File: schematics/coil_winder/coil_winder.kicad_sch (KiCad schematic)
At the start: 2 parts, among them SW1 RotaryEncoder_Switch, U1 Pico

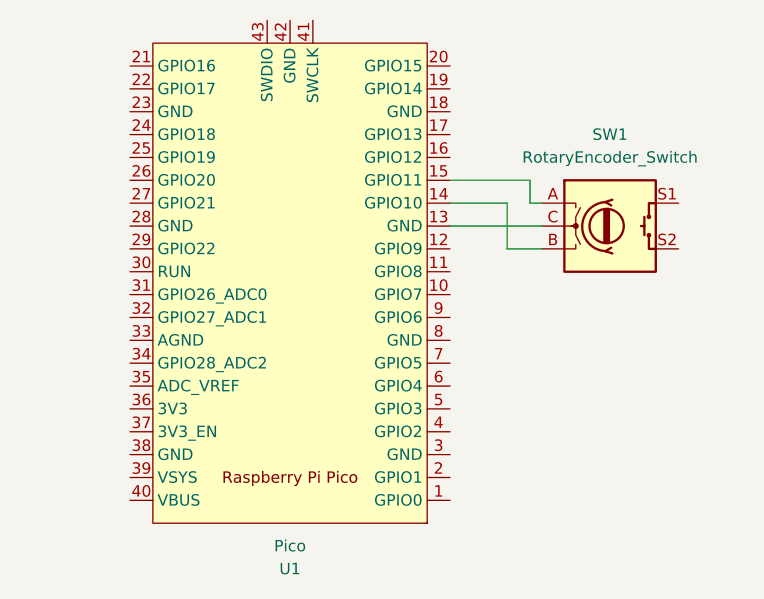
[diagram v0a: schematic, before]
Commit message: Update schematic to include I2C LCD
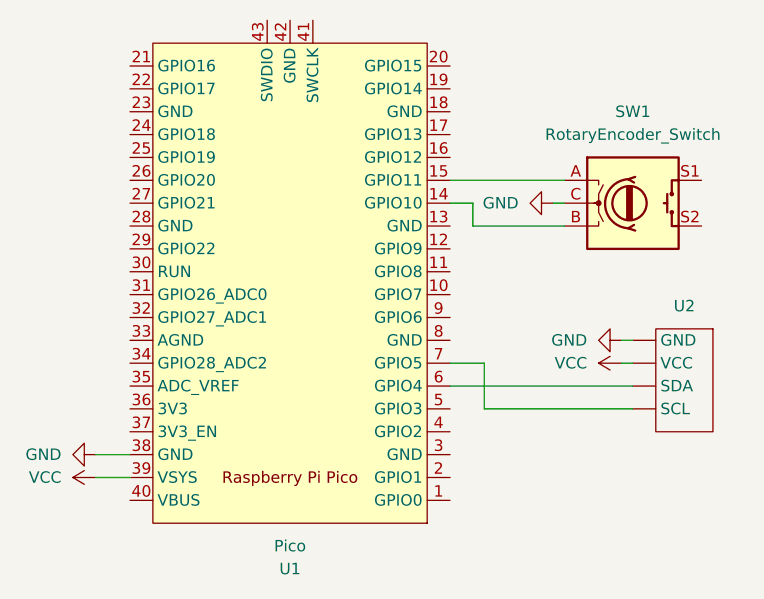
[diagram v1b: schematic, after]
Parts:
- added U2: ~, symbol MCU_RaspberryPi_and_Boards:I2C_LCD
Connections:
- net at U1.13 (GND): no longer SW1.C
- net GND: now reaches U1.38 (GND)
- net GND: now also SW1.C, U2. (VCC)
- net VCC: now reaches U1.39 (VSYS)
- net VCC: now also U2. (VCC)
- net at U1.6 (GPIO4): now also U2. (VCC)
- net at U1.7 (GPIO5): now also U2. (VCC)
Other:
- moved on the sheet: SW1
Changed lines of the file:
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@@
 (kicad_sch (version 20230121) (generator eeschema)
   (paper "A4")
-  (wire (pts (xy 158.75 78.74) (xy 158.75 73.66))
-    (stroke (width 0) (type default))
-  )
-  (wire (pts (xy 158.75 73.66) (xy 152.4 73.66))
-    (stroke (width 0) (type default))
-  )
-  (wire (pts (xy 162.56 73.66) (xy 161.29 73.66))
-    (stroke (width 0) (type default))
-  )
-  (wire (pts (xy 152.4 76.2) (xy 162.56 76.2))
-    (stroke (width 0) (type default))
-  )
-  (wire (pts (xy 161.29 71.12) (xy 152.4 71.12))
-    (stroke (width 0) (type default))
-  )
-  (wire (pts (xy 161.29 73.66) (xy 161.29 71.12))
-    (stroke (width 0) (type default))
-  )
-  (wire (pts (xy 162.56 78.74) (xy 158.75 78.74))
-    (stroke (width 0) (type default))
+  (wire (pts (xy 152.4 93.98) (xy 172.72 93.98))
+    (stroke (width 0) (type default))
+  )
+  (wire (pts (xy 113.03 104.14) (xy 116.84 104.14))
+    (stroke (width 0) (type default))
+  )
+  (wire (pts (xy 156.21 91.44) (xy 152.4 91.44))
+    (stroke (width 0) (type default))
+  )
+  (wire (pts (xy 154.94 73.66) (xy 152.4 73.66))
+    (stroke (width 0) (type default))
+  )
+  (wire (pts (xy 165.1 76.2) (xy 154.94 76.2))
+    (stroke (width 0) (type default))
+  )
+  (wire (pts (xy 156.21 96.52) (xy 156.21 91.44))
+    (stroke (width 0) (type default))
+  )
+  (wire (pts (xy 154.94 76.2) (xy 154.94 73.66))
+    (stroke (width 0) (type default))
+  )
+  (wire (pts (xy 171.45 91.44) (xy 172.72 91.44))
+    (stroke (width 0) (type default))
+  )
+  (wire (pts (xy 163.83 73.66) (xy 165.1 73.66))
+    (stroke (width 0) (type default))
+  )
+  (wire (pts (xy 113.03 101.6) (xy 116.84 101.6))
+    (stroke (width 0) (type default))
+  )
+  (wire (pts (xy 152.4 71.12) (xy 165.1 71.12))
+    (stroke (width 0) (type default))
+  )
+  (wire (pts (xy 172.72 96.52) (xy 156.21 96.52))
+    (stroke (width 0) (type default))
+  )
+  (wire (pts (xy 171.45 88.9) (xy 172.72 88.9))
+    (stroke (width 0) (type default))
+  )
+  (symbol (lib_id "power:VCC") (at 113.03 104.14 90) (unit 1)
+    (in_bom yes) (on_board yes) (dnp no) (fields_autoplaced)
+    (property "Reference" "#PWR04" (at 116.84 104.14 0)
+      (effects (font (size 1.27 1.27)) hide)
+    )
+    (property "Value" "VCC" (at 109.22 104.14 90)
+      (effects (font (size 1.27 1.27)) (justify left))
+    )
+    (property "Footprint" "" (at 113.03 104.14 0)
+      (effects (font (size 1.27 1.27)) hide)
+    )
+    (property "Datasheet" "" (at 113.03 104.14 0)
+      (effects (font (size 1.27 1.27)) hide)
+    )
+    (pin "1")
+    (instances
+      (project "coil_winder"
+        (path "/5ec64e02-ee9b-4809-b355-36a61de13204"
+          (reference "#PWR04") (unit 1)
+        )
+      )
+    )
+  )
+  (symbol (lib_id "power:VCC") (at 171.45 91.44 90) (unit 1)
+    (in_bom yes) (on_board yes) (dnp no) (fields_autoplaced)
+    (property "Reference" "#PWR05" (at 175.26 91.44 0)
+      (effects (font (size 1.27 1.27)) hide)
+    )
+    (property "Value" "VCC" (at 167.64 91.44 90)
+      (effects (font (size 1.27 1.27)) (justify left))
+    )
+    (property "Footprint" "" (at 171.45 91.44 0)
+      (effects (font (size 1.27 1.27)) hide)
+    )
+    (property "Datasheet" "" (at 171.45 91.44 0)
+      (effects (font (size 1.27 1.27)) hide)
+    )
+    (pin "1")
+    (instances
+      (project "coil_winder"
+        (path "/5ec64e02-ee9b-4809-b355-36a61de13204"
+          (reference "#PWR05") (unit 1)
+        )
+      )
+    )
+  )
+  (symbol (lib_id "MCU_RaspberryPi_and_Boards:I2C_LCD") (at 177.8 92.71 0) (mirror y) (unit 1)
+    (in_bom yes) (on_board yes) (dnp no)
+    (property "Reference" "U2" (at 178.435 85.09 0)
+      (effects (font (size 1.27 1.27)))
+    )
+    (property "Value" "~" (at 179.07 86.36 0)
+      (effects (font (size 1.27 1.27)))
+    )
+    (property "Footprint" "" (at 179.07 86.36 0)
+      (effects (font (size 1.27 1.27)) hide)
+    )
+    (property "Datasheet" "" (at 179.07 86.36 0)
+      (effects (font (size 1.27 1.27)) hide)
+    )
+    (pin "")
+    (pin "")
+    (pin "")
+    (pin "")
+    (instances
+      (project "coil_winder"
+        (path "/5ec64e02-ee9b-4809-b355-36a61de13204"
+          (reference "U2") (unit 1)
+        )
+      )
+    )
+  )
+  (symbol (lib_id "power:GND") (at 113.03 101.6 270) (unit 1)
+    (in_bom yes) (on_board yes) (dnp no) (fields_autoplaced)
+    (property "Reference" "#PWR03" (at 106.68 101.6 0)
+      (effects (font (size 1.27 1.27)) hide)
+    )
+    (property "Value" "GND" (at 109.22 101.6 90)
+      (effects (font (size 1.27 1.27)) (justify right))
+    )
+    (property "Footprint" "" (at 113.03 101.6 0)
+      (effects (font (size 1.27 1.27)) hide)
+    )
+    (property "Datasheet" "" (at 113.03 101.6 0)
+      (effects (font (size 1.27 1.27)) hide)
+    )
+    (pin "1")
+    (instances
+      (project "coil_winder"
+        (path "/5ec64e02-ee9b-4809-b355-36a61de13204"
+          (reference "#PWR03") (unit 1)
+        )
+      )
+    )
+  )
+  (symbol (lib_id "power:GND") (at 171.45 88.9 270) (unit 1)
+    (in_bom yes) (on_board yes) (dnp no) (fields_autoplaced)
+    (property "Reference" "#PWR02" (at 165.1 88.9 0)
+      (effects (font (size 1.27 1.27)) hide)
+    )
+    (property "Value" "GND" (at 167.64 88.9 90)
+      (effects (font (size 1.27 1.27)) (justify right))
+    )
+    (property "Footprint" "" (at 171.45 88.9 0)
+      (effects (font (size 1.27 1.27)) hide)
+    )
+    (property "Datasheet" "" (at 171.45 88.9 0)
+      (effects (font (size 1.27 1.27)) hide)
+    )
+    (pin "1")
+    (instances
+      (project "coil_winder"
+        (path "/5ec64e02-ee9b-4809-b355-36a61de13204"
+          (reference "#PWR02") (unit 1)
+        )
+      )
+    )
+  )
+  (symbol (lib_id "power:GND") (at 163.83 73.66 270) (unit 1)
+    (in_bom yes) (on_board yes) (dnp no) (fields_autoplaced)
+    (property "Reference" "#PWR01" (at 157.48 73.66 0)
+      (effects (font (size 1.27 1.27)) hide)
+    )
+    (property "Value" "GND" (at 160.02 73.66 90)
+      (effects (font (size 1.27 1.27)) (justify right))
+    )
+    (property "Footprint" "" (at 163.83 73.66 0)
+      (effects (font (size 1.27 1.27)) hide)
+    )
+    (property "Datasheet" "" (at 163.83 73.66 0)
+      (effects (font (size 1.27 1.27)) hide)
+    )
+    (pin "1")
+    (instances
+      (project "coil_winder"
+        (path "/5ec64e02-ee9b-4809-b355-36a61de13204"
+          (reference "#PWR01") (unit 1)
+        )
+      )
+    )
   )
   (symbol (lib_id "MCU_RaspberryPi_and_Boards:Pico") (at 134.62 82.55 180) (unit 1)
@@
     )
   )
-  (symbol (lib_id "Device:RotaryEncoder_Switch") (at 170.18 76.2 0) (unit 1)
+  (symbol (lib_id "Device:RotaryEncoder_Switch") (at 172.72 73.66 0) (unit 1)
     (in_bom yes) (on_board yes) (dnp no)
-    (property "Reference" "SW1" (at 170.18 66.04 0)
-      (effects (font (size 1.27 1.27)))
-    )
-    (property "Value" "RotaryEncoder_Switch" (at 170.18 68.58 0)
-      (effects (font (size 1.27 1.27)))
-    )
-    (property "Footprint" "" (at 166.37 72.136 0)
-      (effects (font (size 1.27 1.27)) hide)
-    )
-    (property "Datasheet" "~" (at 170.18 69.596 0)
-      (effects (font (size 1.27 1.27)) hide)
-    )
+    (property "Reference" "SW1" (at 172.72 63.5 0)
+      (effects (font (size 1.27 1.27)))
+    )
+    (property "Value" "RotaryEncoder_Switch" (at 172.72 66.04 0)
+      (effects (font (size 1.27 1.27)))
+    )
+    (property "Footprint" "" (at 168.91 69.596 0)
+      (effects (font (size 1.27 1.27)) hide)
+    )
+    (property "Datasheet" "~" (at 172.72 67.056 0)
+      (effects (font (size 1.27 1.27)) hide)
+    )

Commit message: Add stepper motors unconnected to pi
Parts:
- added A1, A2: Pololu_Breakout_A4988, Module:Pololu_Breakout-16_15.2x20.3mm, symbol Driver_Motor:Pololu_Breakout_A4988
- added J1: Stepper_Motor_1, symbol Connector_Generic:Conn_01x04
- added J2: Stepper_Motor_2, symbol Connector_Generic:Conn_01x04
- renumbered U2 to LCD
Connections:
- net GND: now also A1.1 (GND), A1.12 (MS3), A1.7 (GND), A2.1 (GND), A2.12 (MS3), A2.7 (GND)
- net VCC: now also A1.10 (MS1), A1.11 (MS2), A1.2 (VDD), A2.10 (MS1), A2.11 (MS2), A2.2 (VDD)
- new net: A1.3 (1B), J1.1 (Pin_1)
- new net: A1.4 (1A), J1.2 (Pin_2)
- new net: A1.5 (2A), J1.3 (Pin_3)
- new net: A1.6 (2B), J1.4 (Pin_4)
- new net: A1.13 (~{RESET}), A1.14 (~{SLEEP})
- new net: A2.3 (1B), J2.1 (Pin_1)
- new net: A2.4 (1A), J2.2 (Pin_2)
- new net: A2.5 (2A), J2.3 (Pin_3)
- new net: A2.6 (2B), J2.4 (Pin_4)
- new net: A2.13 (~{RESET}), A2.14 (~{SLEEP})
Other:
- moved on the sheet: LCD, SW1, U1

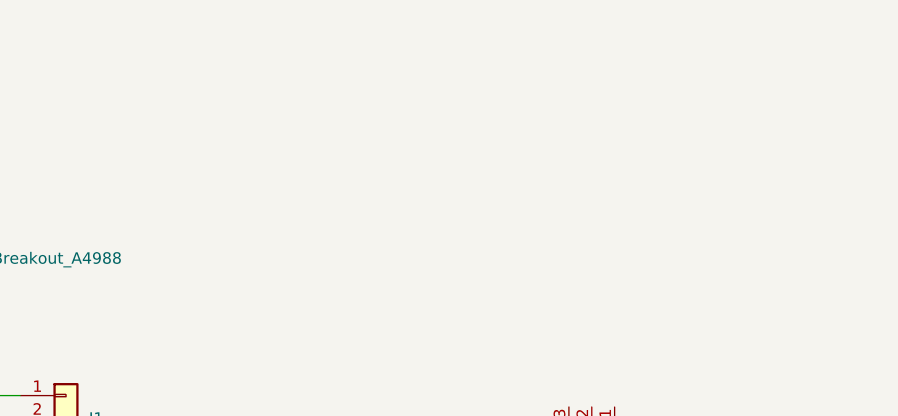
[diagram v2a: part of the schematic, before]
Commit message: Add power circuit
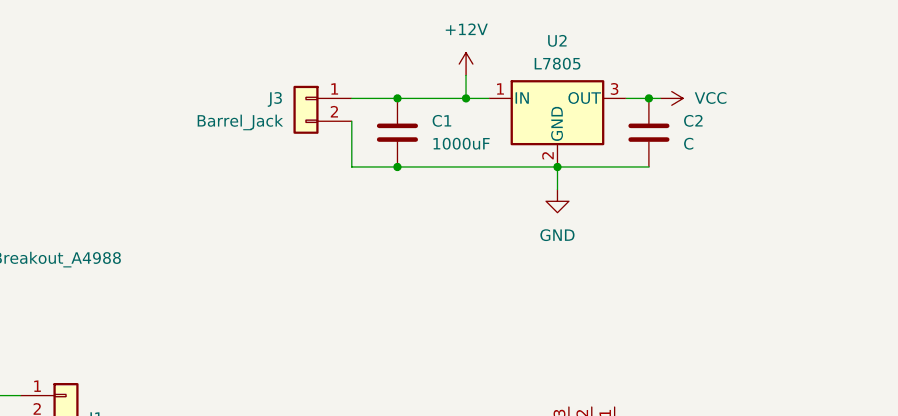
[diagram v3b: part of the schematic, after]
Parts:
- added C1: 1000uF, symbol Device:C
- added C2: C, symbol Device:C
- added J3: Barrel_Jack, symbol Connector_Generic:Conn_01x02
- added U2: L7805, symbol Regulator_Linear:L7805
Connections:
- net GND: now also C1.2, C2.2, J3.2 (Pin_2), U2.2 (GND)
- net VCC: now also C2.1, U2.3 (OUT)
- new net +12V: C1.1, J3.1 (Pin_1), U2.1 (IN)
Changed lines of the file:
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@@
 (kicad_sch (version 20230121) (generator eeschema)
   (paper "A4")
+  (junction (at 143.51 24.13) (diameter 0) (color 0 0 0 0)
+  )
   (junction (at 85.09 146.05) (diameter 0) (color 0 0 0 0)
   )
   (junction (at 73.66 67.31) (diameter 0) (color 0 0 0 0)
   )
+  (junction (at 171.45 24.13) (diameter 0) (color 0 0 0 0)
+  )
+  (junction (at 143.51 31.75) (diameter 0) (color 0 0 0 0)
+  )
   (junction (at 85.09 82.55) (diameter 0) (color 0 0 0 0)
   )
+  (junction (at 151.13 24.13) (diameter 0) (color 0 0 0 0)
+  )
+  (junction (at 161.29 31.75) (diameter 0) (color 0 0 0 0)
+  )
   (junction (at 73.66 130.81) (diameter 0) (color 0 0 0 0)
   )
+  (wire (pts (xy 143.51 24.13) (xy 151.13 24.13))
+    (stroke (width 0) (type default))
+  )
   (wire (pts (xy 72.39 67.31) (xy 73.66 67.31))
     (stroke (width 0) (type default))
@@
     (stroke (width 0) (type default))
   )
+  (wire (pts (xy 151.13 21.59) (xy 151.13 24.13))
+    (stroke (width 0) (type default))
+  )
   (wire (pts (xy 90.17 143.51) (xy 90.17 146.05))
     (stroke (width 0) (type default))
@@
     (stroke (width 0) (type default))
   )
+  (wire (pts (xy 161.29 31.75) (xy 161.29 34.29))
+    (stroke (width 0) (type default))
+  )
   (wire (pts (xy 186.69 96.52) (xy 182.88 96.52))
     (stroke (width 0) (type default))
@@
     (stroke (width 0) (type default))
   )
+  (wire (pts (xy 138.43 26.67) (xy 138.43 31.75))
+    (stroke (width 0) (type default))
+  )
+  (wire (pts (xy 143.51 31.75) (xy 161.29 31.75))
+    (stroke (width 0) (type default))
+  )
   (wire (pts (xy 185.42 81.28) (xy 185.42 78.74))
     (stroke (width 0) (type default))
@@
     (stroke (width 0) (type default))
   )
+  (wire (pts (xy 151.13 24.13) (xy 153.67 24.13))
+    (stroke (width 0) (type default))
+  )
   (wire (pts (xy 143.51 106.68) (xy 147.32 106.68))
     (stroke (width 0) (type default))
@@
     (stroke (width 0) (type default))
   )
+  (wire (pts (xy 168.91 24.13) (xy 171.45 24.13))
+    (stroke (width 0) (type default))
+  )
   (wire (pts (xy 203.2 101.6) (xy 186.69 101.6))
     (stroke (width 0) (type default))
@@
     (stroke (width 0) (type default))
   )
+  (wire (pts (xy 161.29 31.75) (xy 171.45 31.75))
+    (stroke (width 0) (type default))
+  )
   (wire (pts (xy 74.93 113.03) (xy 72.39 113.03))
     (stroke (width 0) (type default))
@@
     (stroke (width 0) (type default))
   )
+  (wire (pts (xy 171.45 24.13) (xy 172.72 24.13))
+    (stroke (width 0) (type default))
+  )
+  (wire (pts (xy 138.43 31.75) (xy 143.51 31.75))
+    (stroke (width 0) (type default))
+  )
   (wire (pts (xy 85.09 143.51) (xy 85.09 146.05))
     (stroke (width 0) (type default))
@@
   )
   (wire (pts (xy 97.79 120.65) (xy 101.6 120.65))
+    (stroke (width 0) (type default))
+  )
+  (wire (pts (xy 138.43 24.13) (xy 143.51 24.13))
     (stroke (width 0) (type default))
   )
@@
     )
   )
+  (symbol (lib_id "power:VCC") (at 172.72 24.13 270) (unit 1)
+    (in_bom yes) (on_board yes) (dnp no) (fields_autoplaced)
+    (property "Reference" "#PWR016" (at 168.91 24.13 0)
+      (effects (font (size 1.27 1.27)) hide)
+    )
+    (property "Value" "VCC" (at 176.53 24.13 90)
+      (effects (font (size 1.27 1.27)) (justify left))
+    )
+    (property "Footprint" "" (at 172.72 24.13 0)
+      (effects (font (size 1.27 1.27)) hide)
+    )
+    (property "Datasheet" "" (at 172.72 24.13 0)
+      (effects (font (size 1.27 1.27)) hide)
+    )
+    (pin "1")
+    (instances
+      (project "coil_winder"
+        (path "/5ec64e02-ee9b-4809-b355-36a61de13204"
+          (reference "#PWR016") (unit 1)
+        )
+      )
+    )
+  )
   (symbol (lib_id "power:VCC") (at 85.09 102.87 0) (unit 1)
     (in_bom yes) (on_board yes) (dnp no) (fields_autoplaced)
@@
     )
   )
+  (symbol (lib_id "power:+12V") (at 151.13 21.59 0) (unit 1)
+    (in_bom yes) (on_board yes) (dnp no) (fields_autoplaced)
+    (property "Reference" "#PWR015" (at 151.13 25.4 0)
+      (effects (font (size 1.27 1.27)) hide)
+    )
+    (property "Value" "+12V" (at 151.13 16.51 0)
+      (effects (font (size 1.27 1.27)))
+    )
+    (property "Footprint" "" (at 151.13 21.59 0)
+      (effects (font (size 1.27 1.27)) hide)
+    )
+    (property "Datasheet" "" (at 151.13 21.59 0)
+      (effects (font (size 1.27 1.27)) hide)
+    )
+    (pin "1")
+    (instances
+      (project "coil_winder"
+        (path "/5ec64e02-ee9b-4809-b355-36a61de13204"
+          (reference "#PWR015") (unit 1)
+        )
+      )
+    )
+  )
   (symbol (lib_id "power:GND") (at 85.09 85.09 0) (unit 1)
     (in_bom yes) (on_board yes) (dnp no) (fields_autoplaced)
@@
         (path "/5ec64e02-ee9b-4809-b355-36a61de13204"
           (reference "#PWR07") (unit 1)
+        )
+      )
+    )
+  )
+  (symbol (lib_id "Device:C") (at 143.51 27.94 0) (unit 1)
+    (in_bom yes) (on_board yes) (dnp no) (fields_autoplaced)
+    (property "Reference" "C1" (at 147.32 26.67 0)
+      (effects (font (size 1.27 1.27)) (justify left))
+    )
+    (property "Value" "1000uF" (at 147.32 29.21 0)
+      (effects (font (size 1.27 1.27)) (justify left))
+    )
+    (property "Footprint" "" (at 144.4752 31.75 0)
+      (effects (font (size 1.27 1.27)) hide)
+    )
+    (property "Datasheet" "~" (at 143.51 27.94 0)
+      (effects (font (size 1.27 1.27)) hide)
+    )
+    (pin "2")
+    (pin "1")
+    (instances
+      (project "coil_winder"
+        (path "/5ec64e02-ee9b-4809-b355-36a61de13204"
+          (reference "C1") (unit 1)
         )
       )
@@
         (path "/5ec64e02-ee9b-4809-b355-36a61de13204"
           (reference "#PWR08") (unit 1)
+        )
+      )
+    )
+  )
+  (symbol (lib_id "Regulator_Linear:L7805") (at 161.29 24.13 0) (unit 1)
+    (in_bom yes) (on_board yes) (dnp no) (fields_autoplaced)
+    (property "Reference" "U2" (at 161.29 17.78 0)
+      (effects (font (size 1.27 1.27)))
+    )
+    (property "Value" "L7805" (at 161.29 20.32 0)
+      (effects (font (size 1.27 1.27)))
+    )
+    (property "Footprint" "" (at 161.925 27.94 0)
+      (effects (font (size 1.27 1.27) italic) (justify left) hide)
+    )
+    (property "Datasheet" "http://www.st.com/content/ccc/resource/technical/document/datasheet/41/4f/b3/b0/12/d4/47/88/CD00000444.pdf/files/CD00000444.pdf/jcr:content/translations/en.CD00000444.pdf" (at 161.29 25.4 0)
+      (effects (font (size 1.27 1.27)) hide)
+    )
+    (pin "2")
+    (pin "3")
+    (pin "1")
+    (instances
+      (project "coil_winder"
+        (path "/5ec64e02-ee9b-4809-b355-36a61de13204"
+          (reference "U2") (unit 1)
         )
       )
@@
     )
   )
+  (symbol (lib_id "Device:C") (at 171.45 27.94 0) (unit 1)
+    (in_bom yes) (on_board yes) (dnp no) (fields_autoplaced)
+    (property "Reference" "C2" (at 175.26 26.67 0)
+      (effects (font (size 1.27 1.27)) (justify left))
+    )
+    (property "Value" "C" (at 175.26 29.21 0)
+      (effects (font (size 1.27 1.27)) (justify left))
+    )
+    (property "Footprint" "" (at 172.4152 31.75 0)
+      (effects (font (size 1.27 1.27)) hide)
+    )
+    (property "Datasheet" "~" (at 171.45 27.94 0)
+      (effects (font (size 1.27 1.27)) hide)
+    )
+    (pin "2")
+    (pin "1")
+    (instances
+      (project "coil_winder"
+        (path "/5ec64e02-ee9b-4809-b355-36a61de13204"
+          (reference "C2") (unit 1)
+        )
+      )
+    )
+  )
   (symbol (lib_id "Driver_Motor:Pololu_Breakout_A4988") (at 85.09 123.19 0) (unit 1)
     (in_bom yes) (on_board yes) (dnp no) (fields_autoplaced)
@@
         (path "/5ec64e02-ee9b-4809-b355-36a61de13204"
           (reference "A2") (unit 1)
+        )
+      )
+    )
+  )
+  (symbol (lib_id "Connector_Generic:Conn_01x02") (at 133.35 24.13 0) (mirror y) (unit 1)
+    (in_bom yes) (on_board yes) (dnp no)
+    (property "Reference" "J3" (at 130.81 24.13 0)
+      (effects (font (size 1.27 1.27)) (justify left))
+    )
+    (property "Value" "Barrel_Jack" (at 130.81 26.67 0)
+      (effects (font (size 1.27 1.27)) (justify left))
+    )
+    (property "Footprint" "" (at 133.35 24.13 0)
+      (effects (font (size 1.27 1.27)) hide)
+    )
+    (property "Datasheet" "~" (at 133.35 24.13 0)
+      (effects (font (size 1.27 1.27)) hide)
+    )
+    (pin "1")
+    (pin "2")
+    (instances
+      (project "coil_winder"
+        (path "/5ec64e02-ee9b-4809-b355-36a61de13204"
+          (reference "J3") (unit 1)
         )
       )
@@
         )
       )
+    )
+  )
+  (symbol (lib_id "power:GND") (at 161.29 34.29 0) (unit 1)
+    (in_bom yes) (on_board yes) (dnp no) (fields_autoplaced)
+    (property "Reference" "#PWR014" (at 161.29 40.64 0)
+      (effects (font (size 1.27 1.27)) hide)
+    )
+    (property "Value" "GND" (at 161.29 39.37 0)
+      (effects (font (size 1.27 1.27)))
+    )
+    (property "Footprint" "" (at 161.29 34.29 0)
+      (effects (font (size 1.27 1.27)) hide)
+    )
+    (property "Datasheet" "" (at 161.29 34.29 0)
+      (effects (font (size 1.27 1.27)) hide)
+    )
+    (pin "1")
+    (instances
+      (project "coil_winder"
+        (path "/5ec64e02-ee9b-4809-b355-36a61de13204"
+          (reference "#PWR014") (unit 1)
+        )
+      )
